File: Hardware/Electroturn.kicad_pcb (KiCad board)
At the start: 2 copper layers, 133.4 x 82.5 mm, 31 parts, among them J1 Encoder Terminal, J2 Stepper Motor Terminal, J3 Screw_Terminal_01x02, SW1 Feed Switch, SW2 Motor Braking Switch, SW3 Mode Right Scroll, SW4 Mode Left Scroll, SW5 Function Btn 1, SW6 Function Btn 2, SW7 Function Btn 2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

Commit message: Some placement work
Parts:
- moved R8 272.6 mm to (198.1, 38.1)
- moved U3 269.0 mm to (122.7, 50.3)
- moved R10 264.4 mm to (201.9, 38.1), turned to 0 degrees
- moved C1 236.4 mm to (190.5, 43.2)
- moved R5 235.9 mm to (118.1, 81.3), turned to 90 degrees
- moved C2 230.2 mm to (199.3, 43.2)
- moved J3 229.0 mm to (106.7, 111.8)
- moved R9 223.9 mm to (215.9, 43.2)
- moved R11 212.7 mm to (223.5, 48.3)
- moved R4 212.3 mm to (160.0, 99.1)
- moved R2 209.8 mm to (176.5, 99.1)
- moved U1 204.4 mm to (160.0, 54.6)
- moved R1 203.6 mm to (176.5, 94.0)
- moved R3 202.1 mm to (160.0, 94.0)
- moved U2 190.7 mm to (200.7, 72.4)
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
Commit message: correcting mislabeled function button
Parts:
- SW7: value Function Btn 2 -> Function Btn 3
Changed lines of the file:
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@@
   (net 43 "unconnected-(DS2-Pad6)")
   (net 44 "/tft_reset")
-  (net 45 "Net-(SW8-PadA)")
-  (net 46 "Net-(SW8-PadB)")
+  (net 45 "Net-(R10-Pad1)")
+  (net 46 "Net-(R11-Pad2)")
   (net 47 "/panelSwitchInterrupt")
   (net 48 "/panelButtonInterrupt")
@@
       (effects (font (size 1 1) (thickness 0.15)))
     )
-    (fp_text value "Function Btn 2" (at 3.75 6.7) (layer "F.Fab")
+    (fp_text value "Function Btn 3" (at 3.75 6.7) (layer "F.Fab")
       (effects (font (size 1 1) (thickness 0.15)))
     )
@@
     (fp_circle (center 0 0) (end -2.54 0) (layer "F.SilkS") (width 0.12) (fill none))
     (pad "A" thru_hole circle locked (at -7.5 -2) (size 1.524 1.524) (drill 1.2) (layers *.Cu *.Mask)
-      (net 45 "Net-(SW8-PadA)") (pinfunction "A") (pintype "passive"))
+      (net 45 "Net-(R10-Pad1)") (pinfunction "A") (pintype "passive"))
     (pad "B" thru_hole circle locked (at -7.5 2) (size 1.524 1.524) (drill 1.2) (layers *.Cu *.Mask)
-      (net 46 "Net-(SW8-PadB)") (pinfunction "B") (pintype "passive"))
+      (net 46 "Net-(R11-Pad2)") (pinfunction "B") (pintype "passive"))
     (pad "C" thru_hole circle locked (at -7.5 0) (size 1.524 1.524) (drill 1.2) (layers *.Cu *.Mask)
       (net 1 "GND") (pinfunction "C") (pintype "passive"))
@@
     (fp_line (start 11.3 -1.8) (end 11.3 1.8) (layer "B.Fab") (width 0.1))
     (pad "1" thru_hole circle (at 0 0 180) (size 2.4 2.4) (drill 1.2) (layers *.Cu *.Mask)
-      (net 45 "Net-(SW8-PadA)") (pintype "passive"))
+      (net 45 "Net-(R10-Pad1)") (pintype "passive"))
     (pad "2" thru_hole oval (at 12.7 0 180) (size 2.4 2.4) (drill 1.2) (layers *.Cu *.Mask)
       (net 30 "/panelEncoder_A") (pintype "passive"))
@@
       (net 38 "+3V3") (pintype "passive"))
     (pad "2" thru_hole oval (at 12.7 0 180) (size 2.4 2.4) (drill 1.2) (layers *.Cu *.Mask)
-      (net 46 "Net-(SW8-PadB)") (pintype "passive"))
+      (net 46 "Net-(R11-Pad2)") (pintype "passive"))
     (model "${KICAD6_3DMODEL_DIR}/Resistor_THT.3dshapes/R_Axial_DIN0411_L9.9mm_D3.6mm_P12.70mm_Horizontal.wrl"
       (offset (xyz 0 0 0))
@@
     (fp_line (start 0 0) (end 1.4 0) (layer "B.Fab") (width 0.1))
     (pad "1" thru_hole circle (at 0 0) (size 2.4 2.4) (drill 1.2) (layers *.Cu *.Mask)
-      (net 45 "Net-(SW8-PadA)") (pintype "passive"))
+      (net 45 "Net-(R10-Pad1)") (pintype "passive"))
     (pad "2" thru_hole oval (at 12.7 0) (size 2.4 2.4) (drill 1.2) (layers *.Cu *.Mask)
       (net 38 "+3V3") (pintype "passive"))
@@
     (fp_line (start 11.3 -1.8) (end 11.3 1.8) (layer "B.Fab") (width 0.1))
     (pad "1" thru_hole circle (at 0 0 180) (size 2.4 2.4) (drill 1.2) (layers *.Cu *.Mask)
-      (net 46 "Net-(SW8-PadB)") (pintype "passive"))
+      (net 46 "Net-(R11-Pad2)") (pintype "passive"))
     (pad "2" thru_hole oval (at 12.7 0 180) (size 2.4 2.4) (drill 1.2) (layers *.Cu *.Mask)
       (net 17 "/panelEncoder_B") (pintype "passive"))

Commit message: Initial placements
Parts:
- moved R9 38.2 mm to (180.3, 57.1)
- moved C2 32.3 mm to (176.6, 66.0), turned to 0 degrees
- moved R11 29.8 mm to (200.7, 67.3)
- moved R8 22.6 mm to (180.3, 52.1)
- moved R10 13.5 mm to (193.0, 48.3)
- moved C1 6.38 mm to (185.4, 47.0)
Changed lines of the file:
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@@
   )
   (footprint "Capacitor_THT:C_Disc_D6.0mm_W2.5mm_P5.00mm" (layer "B.Cu")
-    (at 190.5 43.18 180)
+    (at 185.38 46.99 180)
     (descr "C, Disc series, Radial, pin pitch=5.00mm, , diameter*width=6*2.5mm^2, Capacitor, http://cdn-reichelt.de/documents/datenblatt/B300/DS_KERKO_TC.pdf")
     (tags "C Disc series Radial pin pitch 5.00mm  diameter 6mm width 2.5mm Capacitor")
@@
   )
   (footprint "Resistor_THT:R_Axial_DIN0411_L9.9mm_D3.6mm_P12.70mm_Horizontal" (layer "B.Cu")
-    (at 198.12 38.1 180)
+    (at 180.34 52.07 180)
     (descr "Resistor, Axial_DIN0411 series, Axial, Horizontal, pin pitch=12.7mm, 1W, length*diameter=9.9*3.6mm^2")
     (tags "Resistor Axial_DIN0411 series Axial Horizontal pin pitch 12.7mm 1W length 9.9mm diameter 3.6mm")
@@
   )
   (footprint "Resistor_THT:R_Axial_DIN0411_L9.9mm_D3.6mm_P12.70mm_Horizontal" (layer "B.Cu")
-    (at 223.52 48.26 180)
+    (at 200.66 67.31 180)
     (descr "Resistor, Axial_DIN0411 series, Axial, Horizontal, pin pitch=12.7mm, 1W, length*diameter=9.9*3.6mm^2")
     (tags "Resistor Axial_DIN0411 series Axial Horizontal pin pitch 12.7mm 1W length 9.9mm diameter 3.6mm")
@@
   )
   (footprint "Capacitor_THT:C_Disc_D6.0mm_W2.5mm_P5.00mm" (layer "B.Cu")
-    (at 199.35 43.18 180)
+    (at 176.57 66.04)
     (descr "C, Disc series, Radial, pin pitch=5.00mm, , diameter*width=6*2.5mm^2, Capacitor, http://cdn-reichelt.de/documents/datenblatt/B300/DS_KERKO_TC.pdf")
     (tags "C Disc series Radial pin pitch 5.00mm  diameter 6mm width 2.5mm Capacitor")
@@
     (fp_line (start 5.5 -1.25) (end 5.5 1.25) (layer "B.Fab") (width 0.1))
     (fp_line (start -0.5 -1.25) (end 5.5 -1.25) (layer "B.Fab") (width 0.1))
-    (pad "1" thru_hole circle (at 0 0 180) (size 1.6 1.6) (drill 0.8) (layers *.Cu *.Mask)
+    (pad "1" thru_hole circle (at 0 0) (size 1.6 1.6) (drill 0.8) (layers *.Cu *.Mask)
       (net 17 "/panelEncoder_B") (pintype "passive"))
-    (pad "2" thru_hole circle (at 5 0 180) (size 1.6 1.6) (drill 0.8) (layers *.Cu *.Mask)
+    (pad "2" thru_hole circle (at 5 0) (size 1.6 1.6) (drill 0.8) (layers *.Cu *.Mask)
       (net 1 "GND") (pintype "passive"))
     (model "${KICAD6_3DMODEL_DIR}/Capacitor_THT.3dshapes/C_Disc_D6.0mm_W2.5mm_P5.00mm.wrl"
@@
   )
   (footprint "Resistor_THT:R_Axial_DIN0411_L9.9mm_D3.6mm_P12.70mm_Horizontal" (layer "B.Cu")
-    (at 201.93 38.1)
+    (at 193.04 48.26)
     (descr "Resistor, Axial_DIN0411 series, Axial, Horizontal, pin pitch=12.7mm, 1W, length*diameter=9.9*3.6mm^2")
     (tags "Resistor Axial_DIN0411 series Axial Horizontal pin pitch 12.7mm 1W length 9.9mm diameter 3.6mm")
@@
   )
   (footprint "Resistor_THT:R_Axial_DIN0411_L9.9mm_D3.6mm_P12.70mm_Horizontal" (layer "B.Cu")
-    (at 215.9 43.18 180)
-    (descr "Resistor, Axial_DIN0411 series, Axial, Horizontal, pin pitch=12.7mm, 1W, length*diameter=9.9*3.6mm^2")
-    (tags "Resistor Axial_DIN0411 series Axial Horizontal pin pitch 12.7mm 1W length 9.9mm diameter 3.6mm")
+    (at 180.34 57.15 180)
+    (descr "Resistor, Axial_DIN0411 series, Axial, Horizontal, pin pitch=12.7mm, 1W, length*diameter=9.9*3.6mm^2")
+    (tags "Resistor Axial_DIN0411 series Axial Horizontal pin pitch 12.7mm 1W length 9.9mm diameter 3.6mm")

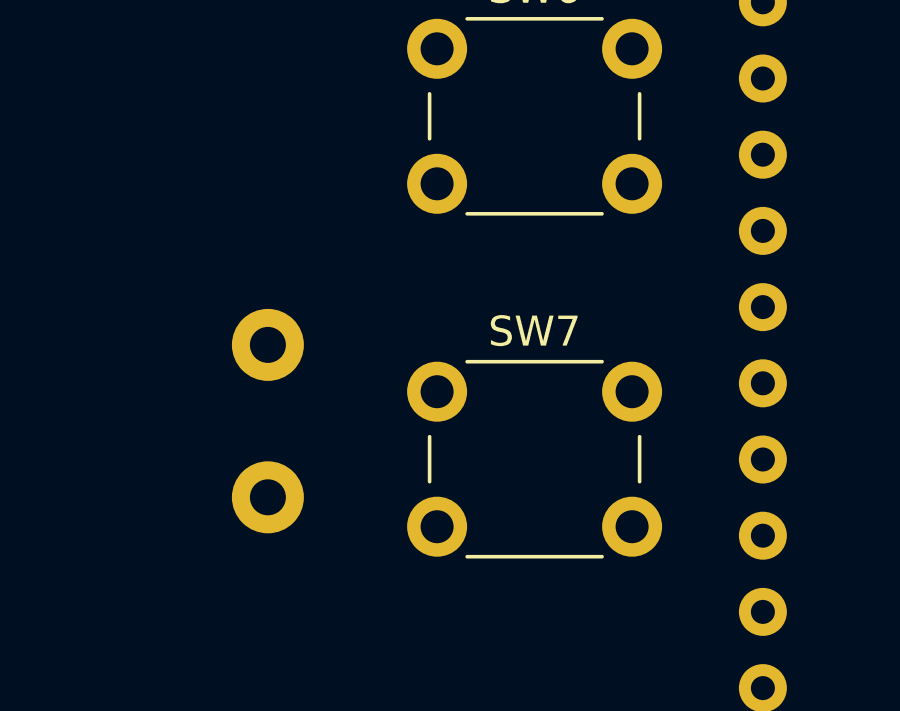
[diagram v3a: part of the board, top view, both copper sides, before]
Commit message: Adding net classes for PCB traces
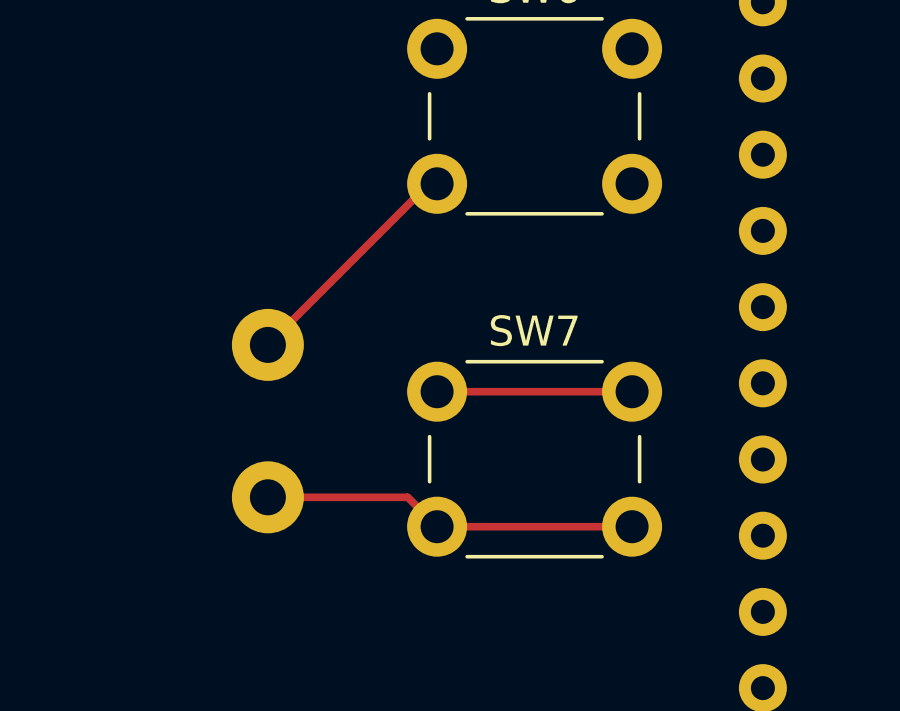
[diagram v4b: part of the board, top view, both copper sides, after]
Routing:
- net GND: track 0.00 -> 20.4 mm
- net Net-(SW7-Pad1): track 0.00 -> 6.50 mm
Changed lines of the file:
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@@
   )
   (gr_rect (start 76.2 114.3) (end 209.55 31.75) (layer "Edge.Cuts") (width 0.15) (fill none))
+  (segment (start 181.9 88.61) (end 182.17 88.61) (width 0.254) (layer "F.Cu") (net 1))
+  (segment (start 181.19 99.06) (end 182.17 100.04) (width 0.254) (layer "F.Cu") (net 1))
+  (segment (start 176.53 99.06) (end 181.19 99.06) (width 0.254) (layer "F.Cu") (net 1))
+  (segment (start 176.53 93.98) (end 181.9 88.61) (width 0.254) (layer "F.Cu") (net 1))
+  (segment (start 182.17 100.04) (end 188.67 100.04) (width 0.254) (layer "F.Cu") (net 1))
+  (segment (start 188.67 95.54) (end 182.17 95.54) (width 0.254) (layer "F.Cu") (net 53))
 )

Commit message: Fixing schematic parity issues with PCB footprints
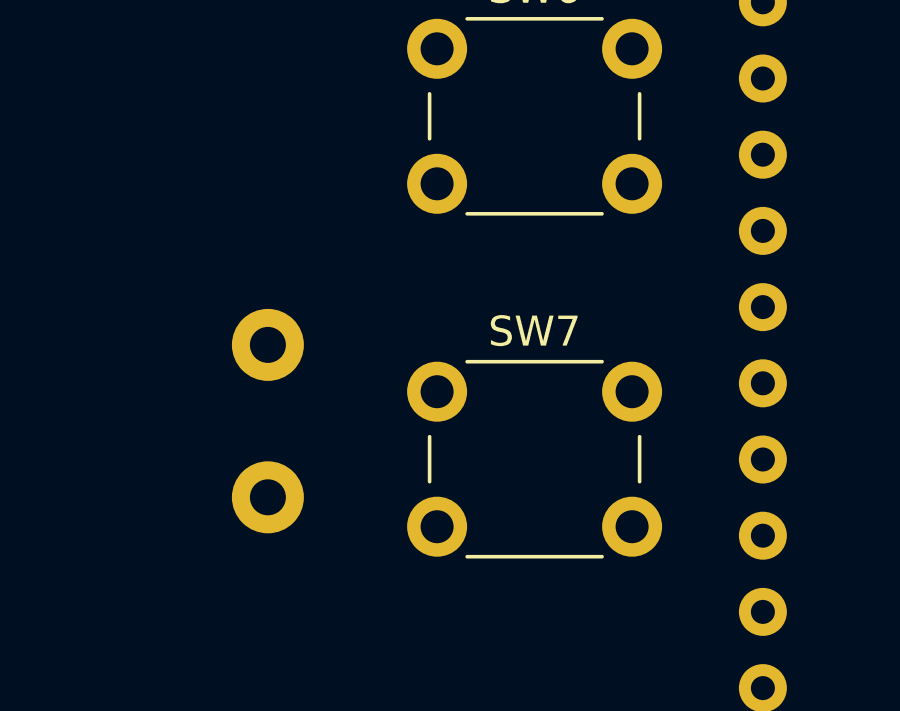
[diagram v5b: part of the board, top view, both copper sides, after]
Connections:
- SW2 pad 4: (no net) -> Net-(SW2-Pad4)
- SW2 pad A: (no net) -> GND
- U2 pad 3: Net-(SW2-Pad3) -> Net-(SW2-Pad4)
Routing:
- net GND: track 20.4 -> 0.00 mm
- net Net-(SW7-Pad1): track 6.50 -> 0.00 mm

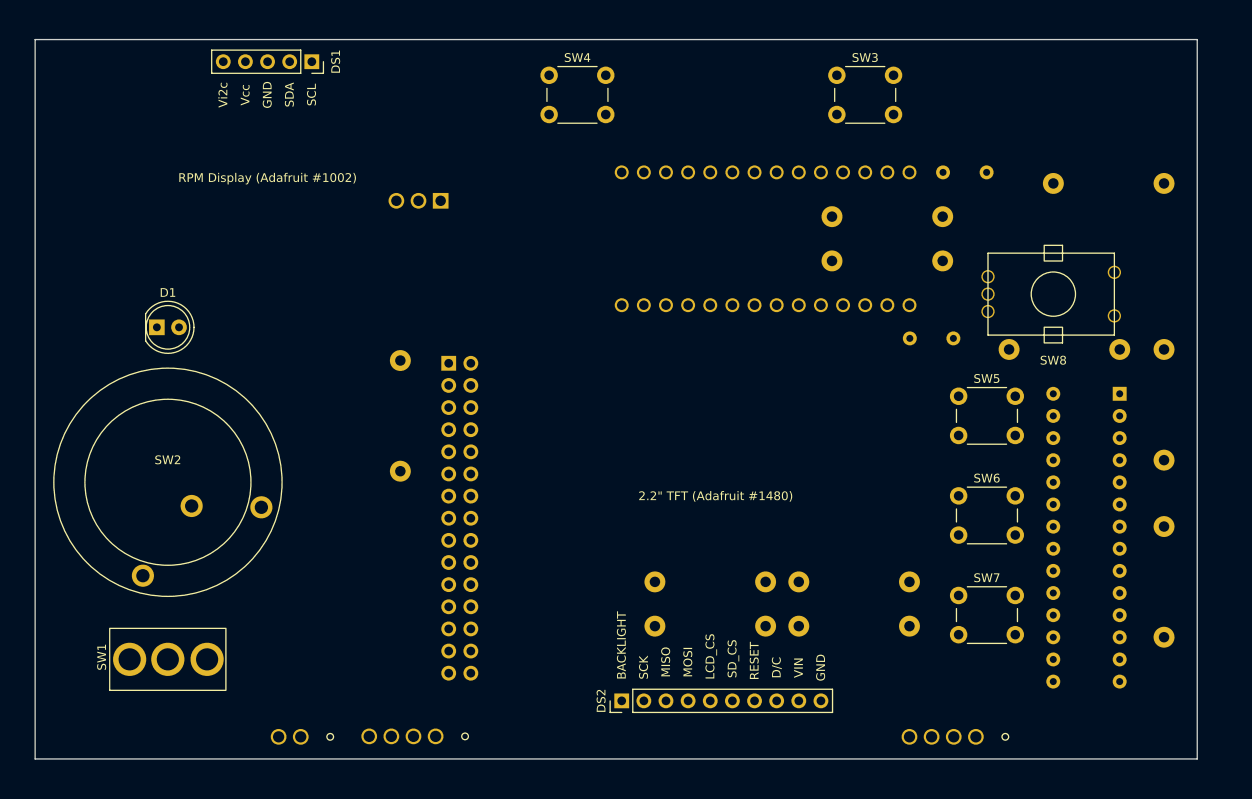
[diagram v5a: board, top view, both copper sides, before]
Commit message: PCB is routed
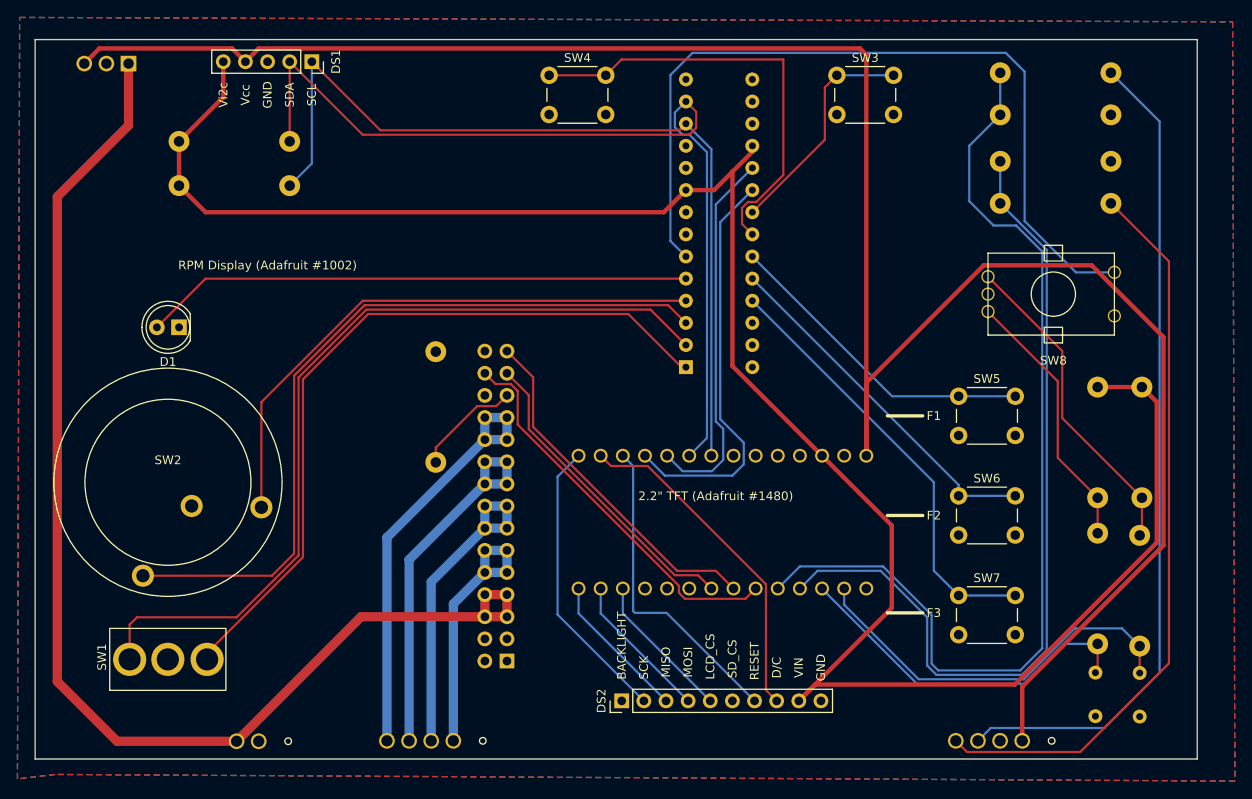
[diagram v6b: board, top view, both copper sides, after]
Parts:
- SW8: value Control Panel Encoder -> locked
- moved R7 115.3 mm to (105.4, 43.4), turned to 180 degrees
- moved R6 105.2 mm to (105.4, 48.5), turned to 180 degrees
- moved C1 64.9 mm to (202.9, 109.4), turned to 90 degrees
- moved R3 64.3 mm to (186.9, 35.6), turned to 0 degrees
- moved R1 58.4 mm to (199.6, 40.4)
- moved R2 58.1 mm to (199.6, 45.7)
- moved R4 55.5 mm to (186.9, 50.5), turned to 0 degrees
- moved U2 49.9 mm to (150.9, 69.3), turned to 0 degrees
- moved C2 43.9 mm to (197.9, 104.4), turned to -90 degrees
- moved R8 43.0 mm to (202.9, 88.6), turned to -90 degrees
- moved U3 39.1 mm to (86.9, 34.5)
- moved R10 37.5 mm to (203.2, 84.3), turned to 90 degrees
- moved R9 35.9 mm to (198.1, 88.4), turned to -90 degrees
- moved A1 34.8 mm to (130.3, 103.1), turned to 0 degrees
- moved U1 32.9 mm to (155.1, 87.1)
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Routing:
- net +5V: track 0.00 -> 242.5 mm
- net +3V3: track 0.00 -> 231.9 mm
- net +24V: track 0.00 -> 142.3 mm
- net Net-(R1-Pad2): track 0.00 -> 113.2 mm
- net /i2c_data: track 0.00 -> 107.1 mm
- net /i2c_clock: track 0.00 -> 101.1 mm
- net Net-(R2-Pad2): track 0.00 -> 96.8 mm
- net Net-(SW1-Pad1): track 0.00 -> 96.4 mm
- net /SpindleEnc_A: track 0.00 -> 95.2 mm
- net Net-(SW8-PadS1): track 0.00 -> 94.0 mm
- net Net-(SW2-Pad4): track 0.00 -> 88.0 mm
- net Net-(SW1-Pad3): track 0.00 -> 86.3 mm
- net /SpindleEnc_B: track 0.00 -> 84.7 mm
- net Net-(SW2-Pad1): track 0.00 -> 65.6 mm
- net Net-(D1-Pad2): track 0.00 -> 63.0 mm
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- added copper zone on B.Cu, net GND
- added copper zone on F.Cu, net GND
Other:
- board text added: "F1"
- board text added: "F2"
- board text added: "F3"

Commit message: Adding mounting holes, starting to generate gerbers
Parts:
- added H1: MountingHole, MountingHole:MountingHole_3.2mm_M3, F.Cu at (206.5, 111.3)
- added H2: MountingHole, MountingHole:MountingHole_3.2mm_M3, F.Cu at (79.2, 111.3)
- added H3: MountingHole, MountingHole:MountingHole_3.2mm_M3, F.Cu at (206.5, 34.8)
- added H4: MountingHole, MountingHole:MountingHole_3.2mm_M3, F.Cu at (79.5, 34.8)
- moved U3 18.8 mm to (87.4, 53.3)
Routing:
- net +24V: track 142.3 -> 122.1 mm
- net +5V: track 242.5 -> 254.4 mm
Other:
- board text added: "+24V"
- board text added: "+5V"
- board text added: "5V Reg."
- board text added: "A"
- board text added: "A-"
- board text added: "B"
- board text added: "B-"
- board text added: "Beth Anne Burford Hampton Morgan Karson Shields"
- board text added: "DC IN"
- board text added: "Designed in Auburn, AL"
- board text added: "ELECTROTURN Electronic Leadscrew System"
- board text added: "GND"
- board text added: "Spindle Encoder"
- board text added: "Stepper"
